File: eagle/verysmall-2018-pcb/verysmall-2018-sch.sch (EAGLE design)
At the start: 14 parts, among them IC1 7805, U1 ESP-WROOM-32, U2 AMS1117-3.3, U3 GY-521MPU6050

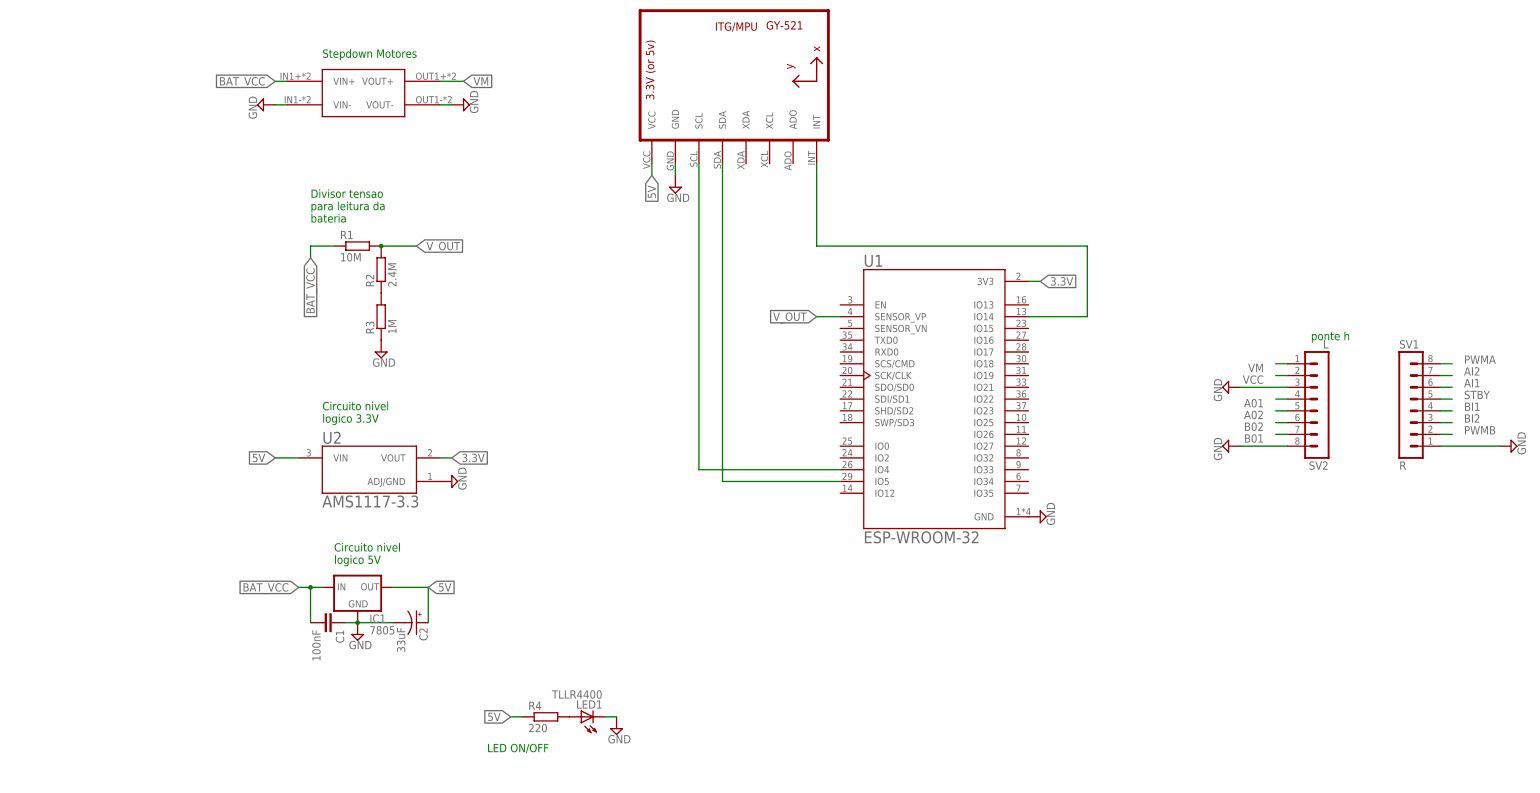
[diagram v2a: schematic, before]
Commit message: Adição dos pinos dos motores e do switch button
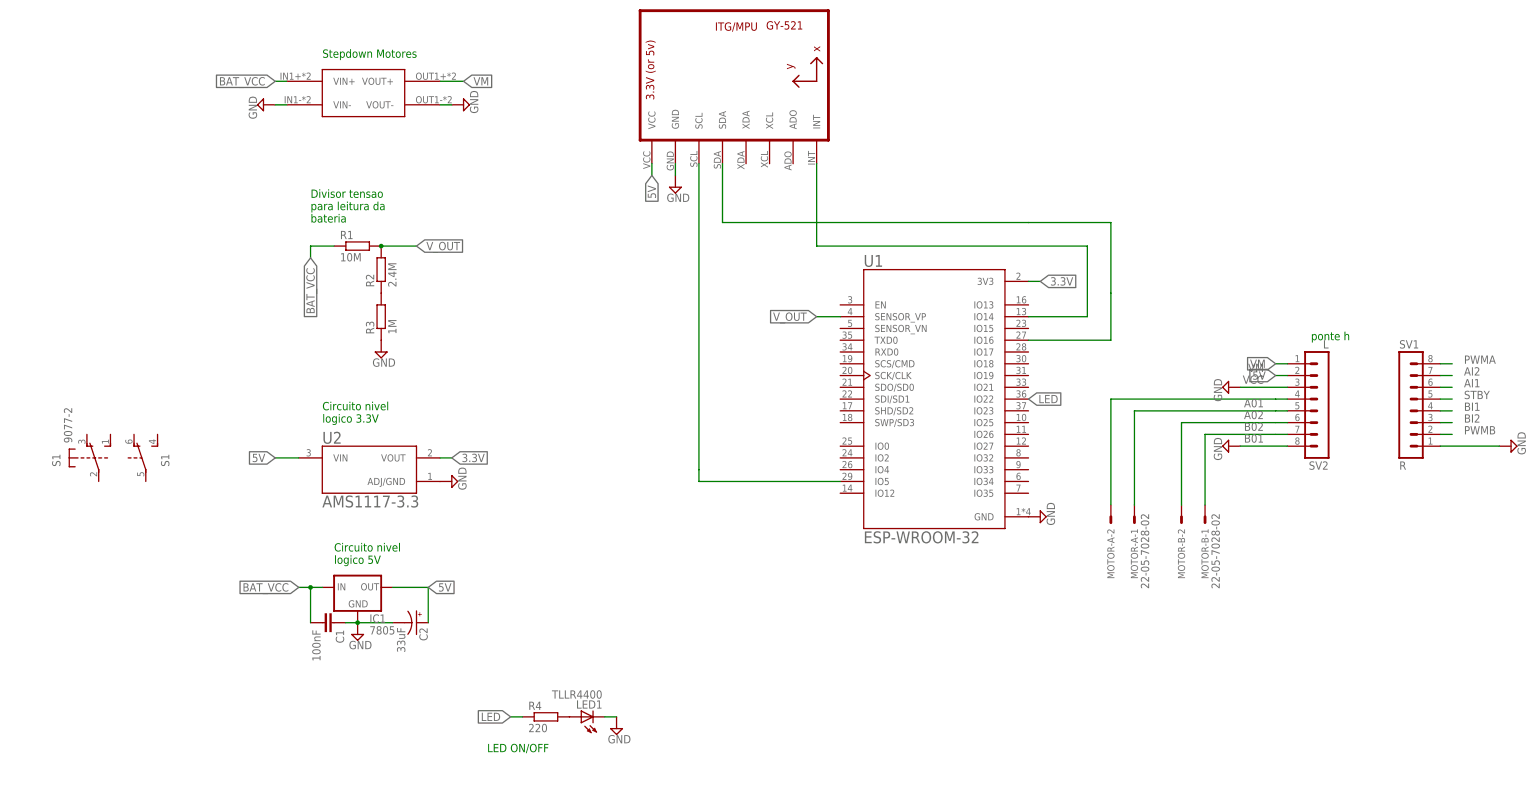
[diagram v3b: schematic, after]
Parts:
- added MOTOR-A, MOTOR-B: 22-05-7028-02, con-molex:22-05-7028-02
- added S1: 9077-2, switch-misc:9077-2
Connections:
- new net LED: R4.1
- net 5V: no longer R4.1
- net A01: now also MOTOR-A-2.S
- net A02: now also MOTOR-A-1.S
- net B01: now also MOTOR-B-1.S
- net B02: now also MOTOR-B-2.S
- net N$1: now also U1.IO5; no longer U1.IO4
- net N$3: now also U1.IO16; no longer U1.IO5
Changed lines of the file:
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@@
 <?xml version="1.0" encoding="utf-8"?>
 <!DOCTYPE eagle SYSTEM "eagle.dtd">
-<eagle version="9.1.2">
+<eagle version="9.1.0">
 <drawing>
 <settings>
@@
 <part name="R4" library="rcl" library_urn="urn:adsk.eagle:library:334" deviceset="R-EU_" device="0207/7" package3d_urn="urn:adsk.eagle:package:23493/1" value="220"/>
 <part name="SUPPLY11" library="supply2" library_urn="urn:adsk.eagle:library:372" deviceset="GND" device=""/>
+<part name="MOTOR-A" library="con-molex" library_urn="urn:adsk.eagle:library:165" deviceset="22-?-02" device="05-7028"/>
+<part name="MOTOR-B" library="con-molex" library_urn="urn:adsk.eagle:library:165" deviceset="22-?-02" device="05-7028"/>
+<part name="S1" library="switch-misc" library_urn="urn:adsk.eagle:library:376" deviceset="9077-2" device="" package3d_urn="urn:adsk.eagle:package:27425/1"/>
 </parts>
 <sheets>
@@
 <instance part="R4" gate="G$1" x="-63.5" y="2.54"/>
 <instance part="SUPPLY11" gate="GND" x="-48.26" y="0"/>
+<instance part="MOTOR-A" gate="-1" x="63.5" y="45.72" rot="R270"/>
+<instance part="MOTOR-A" gate="-2" x="58.42" y="45.72" rot="R270"/>
+<instance part="MOTOR-B" gate="-1" x="78.74" y="45.72" smashed="yes" rot="R270">
+<attribute name="NAME" x="77.978" y="43.18" size="1.524" layer="95" rot="R270"/>
+<attribute name="VALUE" x="80.137" y="46.482" size="1.778" layer="96" rot="R270"/>
+</instance>
+<instance part="MOTOR-B" gate="-2" x="73.66" y="45.72" rot="R270"/>
+<instance part="S1" gate="1" x="-160.02" y="58.42"/>
+<instance part="S1" gate="2" x="-149.86" y="58.42"/>
 </instances>
 <busses>
@@
 <pinref part="C2" gate="G$1" pin="+"/>
 <wire x1="-88.9" y1="22.86" x2="-88.9" y2="30.48" width="0.1524" layer="91"/>
+<label x="93.98" y="76.2" size="1.778" layer="95" rot="R180" xref="yes"/>
 </segment>
 <segment>
@@
 <label x="-40.64" y="119.38" size="1.778" layer="95" rot="R270" xref="yes"/>
 </segment>
-<segment>
-<pinref part="R4" gate="G$1" pin="1"/>
-<wire x1="-68.58" y1="2.54" x2="-71.12" y2="2.54" width="0.1524" layer="91"/>
-<label x="-71.12" y="2.54" size="1.778" layer="95" rot="R180" xref="yes"/>
-</segment>
 </net>
 <net name="N$1" class="0">
 <segment>
-<pinref part="U1" gate="G$1" pin="IO4"/>
-<wire x1="0" y1="55.88" x2="-30.48" y2="55.88" width="0.1524" layer="91"/>
 <pinref part="U3" gate="G$1" pin="SCL"/>
 <wire x1="-30.48" y1="55.88" x2="-30.48" y2="121.92" width="0.1524" layer="91"/>
-</segment>
-</net>
-<net name="N$3" class="0">
-<segment>
-<pinref part="U3" gate="G$1" pin="SDA"/>
 <pinref part="U1" gate="G$1" pin="IO5"/>
-<wire x1="-25.4" y1="121.92" x2="-25.4" y2="53.34" width="0.1524" layer="91"/>
-<wire x1="-25.4" y1="53.34" x2="0" y2="53.34" width="0.1524" layer="91"/>
+<wire x1="-30.48" y1="55.88" x2="-30.48" y2="53.34" width="0.1524" layer="91"/>
+<wire x1="-30.48" y1="53.34" x2="0" y2="53.34" width="0.1524" layer="91"/>
 </segment>
 </net>
@@
 <wire x1="-86.36" y1="139.7" x2="-81.28" y2="139.7" width="0.1524" layer="91"/>
 <label x="-81.28" y="139.7" size="1.778" layer="95" xref="yes"/>
+<label x="93.98" y="78.74" size="1.778" layer="95" rot="R180" xref="yes"/>
 </segment>
 <segment>
@@
 <wire x1="96.52" y1="71.12" x2="93.98" y2="71.12" width="0.1524" layer="91"/>
 <label x="91.44" y="71.12" size="1.778" layer="95" rot="R180"/>
+<pinref part="MOTOR-A" gate="-2" pin="S"/>
+<wire x1="58.42" y1="48.26" x2="58.42" y2="71.12" width="0.1524" layer="91"/>
+<wire x1="58.42" y1="71.12" x2="93.98" y2="71.12" width="0.1524" layer="91"/>
 </segment>
 </net>
@@
 <wire x1="96.52" y1="68.58" x2="93.98" y2="68.58" width="0.1524" layer="91"/>
 <label x="91.44" y="68.58" size="1.778" layer="95" rot="R180"/>
+<pinref part="MOTOR-A" gate="-1" pin="S"/>
+<wire x1="63.5" y1="48.26" x2="63.5" y2="68.58" width="0.1524" layer="91"/>
+<wire x1="63.5" y1="68.58" x2="93.98" y2="68.58" width="0.1524" layer="91"/>
 </segment>
 </net>
@@
 <wire x1="96.52" y1="66.04" x2="93.98" y2="66.04" width="0.1524" layer="91"/>
 <label x="91.44" y="66.04" size="1.778" layer="95" rot="R180"/>
+<pinref part="MOTOR-B" gate="-2" pin="S"/>
+<wire x1="73.66" y1="48.26" x2="73.66" y2="66.04" width="0.1524" layer="91"/>
+<wire x1="73.66" y1="66.04" x2="93.98" y2="66.04" width="0.1524" layer="91"/>
 </segment>
 </net>
@@
 <wire x1="96.52" y1="63.5" x2="93.98" y2="63.5" width="0.1524" layer="91"/>
 <label x="91.44" y="63.5" size="1.778" layer="95" rot="R180"/>
+<pinref part="MOTOR-B" gate="-1" pin="S"/>
+<wire x1="78.74" y1="48.26" x2="78.74" y2="63.5" width="0.1524" layer="91"/>
+<wire x1="78.74" y1="63.5" x2="93.98" y2="63.5" width="0.1524" layer="91"/>
 </segment>
 </net>
@@
 </segment>
 </net>
+<net name="LED" class="0">
+<segment>
+<pinref part="R4" gate="G$1" pin="1"/>
+<wire x1="-68.58" y1="2.54" x2="-71.12" y2="2.54" width="0.1524" layer="91"/>
+<label x="-71.12" y="2.54" size="1.778" layer="95" rot="R180" xref="yes"/>
+<label x="40.64" y="71.12" size="1.778" layer="95" xref="yes"/>
+</segment>
+</net>
+<net name="N$3" class="0">
+<segment>
+<pinref part="U3" gate="G$1" pin="SDA"/>
+<wire x1="-25.4" y1="121.92" x2="-25.4" y2="109.22" width="0.1524" layer="91"/>
+<wire x1="-25.4" y1="109.22" x2="40.64" y2="109.22" width="0.1524" layer="91"/>
+<wire x1="40.64" y1="109.22" x2="58.42" y2="109.22" width="0.1524" layer="91"/>
+<wire x1="58.42" y1="109.22" x2="58.42" y2="93.98" width="0.1524" layer="91"/>
+<pinref part="U1" gate="G$1" pin="IO16"/>
+<wire x1="58.42" y1="93.98" x2="58.42" y2="83.82" width="0.1524" layer="91"/>
+<wire x1="58.42" y1="83.82" x2="40.64" y2="83.82" width="0.1524" layer="91"/>
+</segment>
+</net>

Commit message: Esquematico pronto
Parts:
- added BAT, CHG, RX-TX: 22-05-7028-02, con-molex:22-05-7028-02
- added C3, C5: 100nF, rcl:C-EU075-032X103
- added C4, C6: 10uF, rcl:CPOL-USE2-5
- added Q1: BC548, transistor-npn:BC548
- added R5: 2K2, eagle-ltspice:R0207/10
- added SG1: F/HMB, buzzer:F/HMB
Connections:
- new net BUZZER: R5.1
- new net N$10: U1.IO27
- new net N$11: U1.IO25
- new net N$12: U1.IO32
- new net N$13: U1.IO34
- new net N$14: U1.IO35
- new net N$15: RX-TX-2.S, U1.TXD0
- new net N$16: RX-TX-1.S, U1.RXD0
- new net N$17: Q1.C, SG1.-
- new net N$18: Q1.B, R5.2
- new net N$6: CHG-2.S, S11.S, S12.S
- new net N$7: S11.O, S12.O
- new net N$8: BAT-2.S, S11.P, S12.P
- new net N$9: U1.IO12
- net 3.3V: now also C4.+
- net 5V: now also C5.2
- net BAT_VCC: now also C3.2
- net GND: now also BAT-1.S, C3.1, C4.-, C5.1, C6.-, CHG-1.S, Q1.E
- net VM: now also C6.+

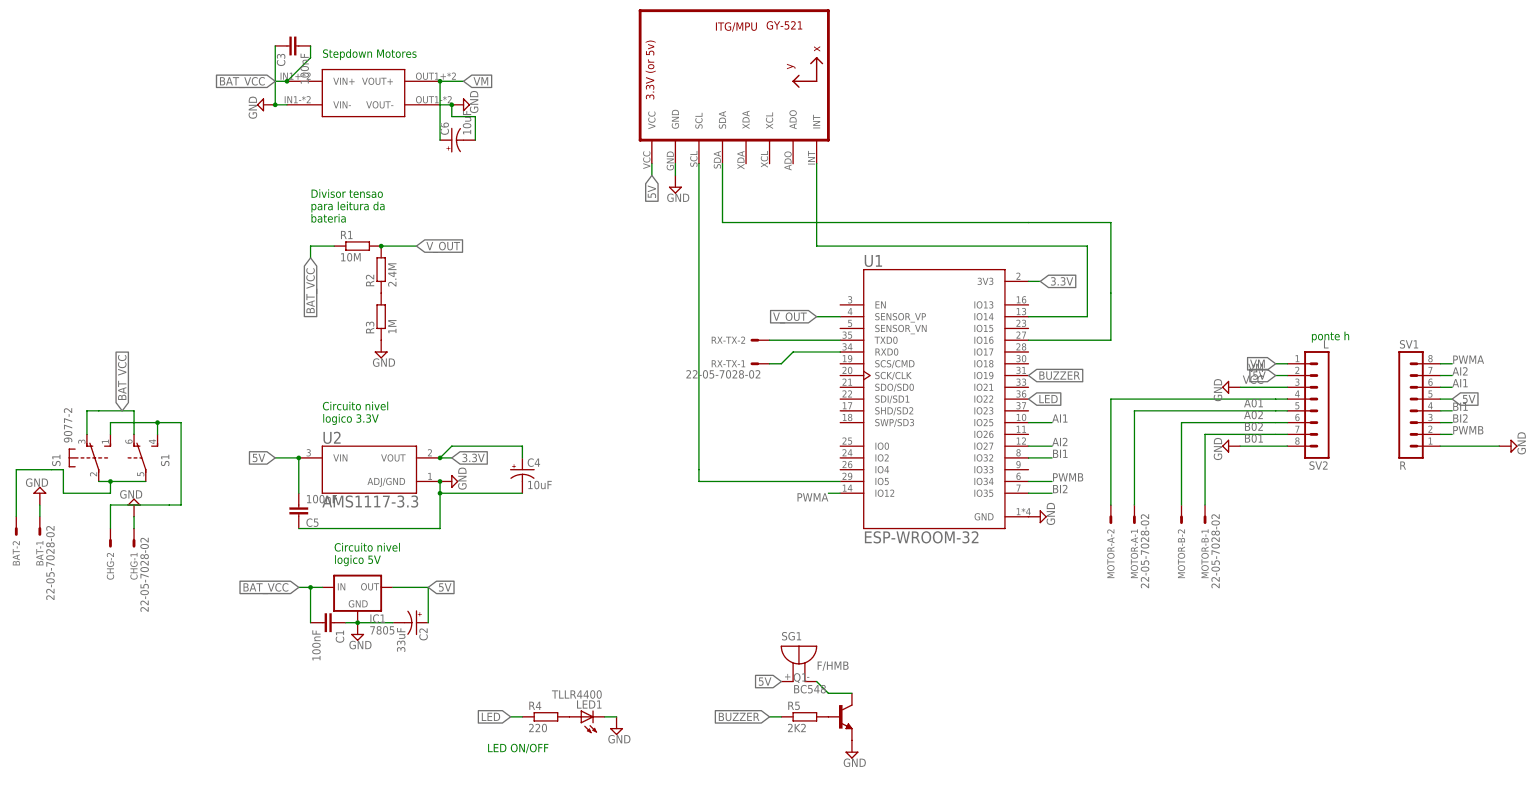
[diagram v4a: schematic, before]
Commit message: ajuste de lable
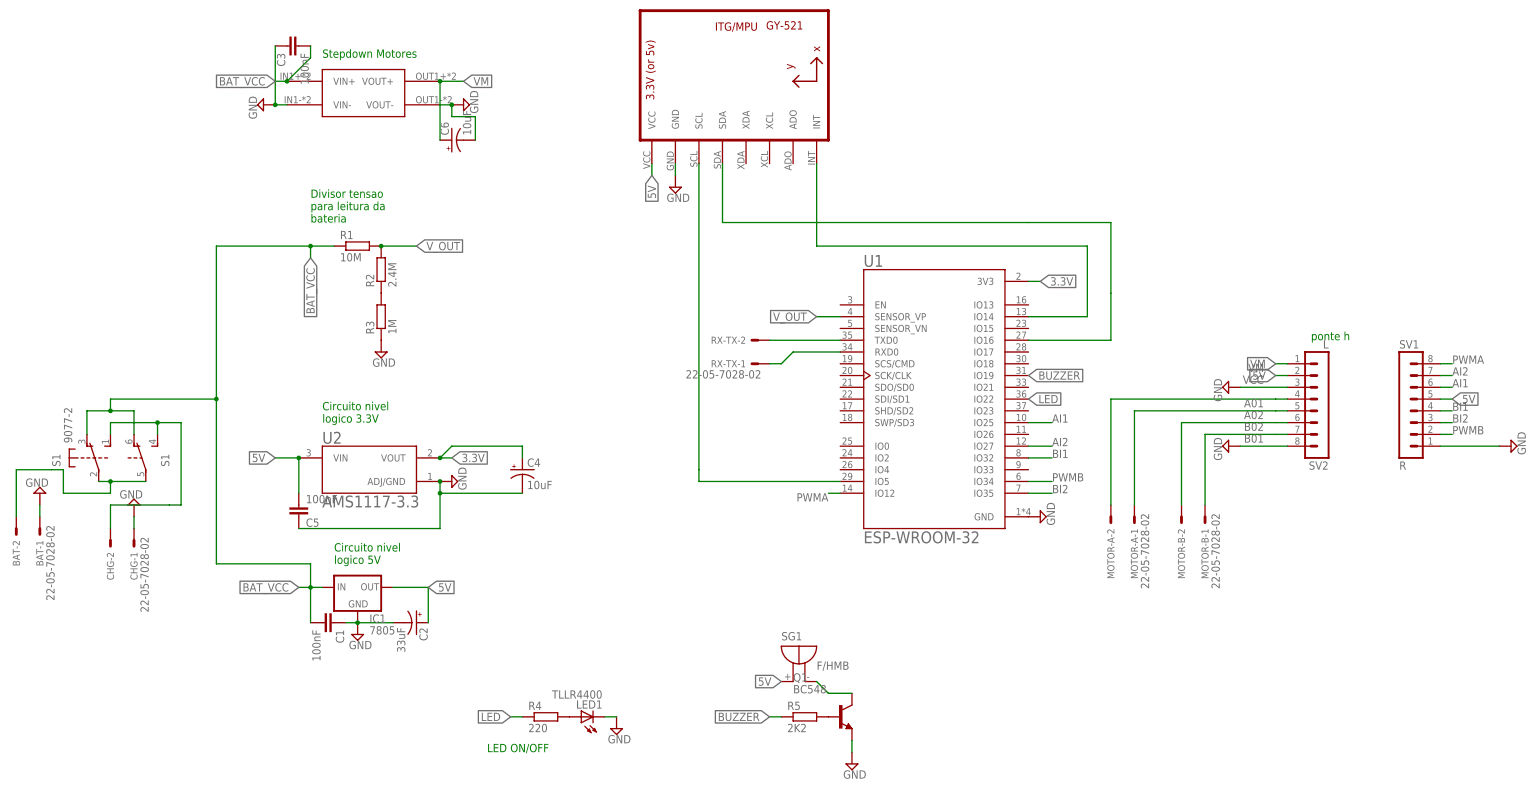
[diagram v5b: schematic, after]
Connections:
- removed net N$7: S11.O, S12.O
- net BAT_VCC: now also S11.O, S12.O
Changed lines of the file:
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@@
 <instance part="SG1" gate="G$1" x="-10.16" y="12.7"/>
 <instance part="Q1" gate="G$1" x="0" y="2.54"/>
-<instance part="SUPPLY14" gate="GND" x="2.54" y="-5.08"/>
+<instance part="SUPPLY14" gate="GND" x="2.54" y="-7.62"/>
 <instance part="R5" gate="G$1" x="-7.62" y="2.54"/>
 </instances>
@@
 <pinref part="Q1" gate="G$1" pin="E"/>
 <pinref part="SUPPLY14" gate="GND" pin="GND"/>
+<wire x1="2.54" y1="-5.08" x2="2.54" y2="-2.54" width="0.1524" layer="91"/>
 </segment>
 </net>
@@
 </net>
 <net name="BAT_VCC" class="0">
-<segment>
-<pinref part="R1" gate="G$1" pin="1"/>
-<wire x1="-109.22" y1="104.14" x2="-114.3" y2="104.14" width="0.1524" layer="91"/>
-<label x="-114.3" y="101.6" size="1.778" layer="95" rot="R270" xref="yes"/>
-<wire x1="-114.3" y1="101.6" x2="-114.3" y2="104.14" width="0.1524" layer="91"/>
-</segment>
 <segment>
 <pinref part="IC1" gate="A" pin="IN"/>
@@
 <wire x1="-114.3" y1="22.86" x2="-114.3" y2="30.48" width="0.1524" layer="91"/>
 <junction x="-114.3" y="30.48"/>
-<label x="-154.94" y="68.58" size="1.778" layer="95" rot="R90" xref="yes"/>
+<wire x1="-134.62" y1="104.14" x2="-134.62" y2="71.12" width="0.1524" layer="91"/>
+<wire x1="-134.62" y1="71.12" x2="-134.62" y2="35.56" width="0.1524" layer="91"/>
+<wire x1="-134.62" y1="35.56" x2="-114.3" y2="35.56" width="0.1524" layer="91"/>
+<wire x1="-114.3" y1="35.56" x2="-114.3" y2="30.48" width="0.1524" layer="91"/>
+<pinref part="R1" gate="G$1" pin="1"/>
+<wire x1="-109.22" y1="104.14" x2="-114.3" y2="104.14" width="0.1524" layer="91"/>
+<label x="-114.3" y="101.6" size="1.778" layer="95" rot="R270" xref="yes"/>
+<wire x1="-114.3" y1="101.6" x2="-114.3" y2="104.14" width="0.1524" layer="91"/>
+<wire x1="-134.62" y1="104.14" x2="-114.3" y2="104.14" width="0.1524" layer="91"/>
+<junction x="-114.3" y="104.14"/>
+<pinref part="S1" gate="1" pin="O"/>
+<wire x1="-162.56" y1="68.58" x2="-162.56" y2="63.5" width="0.1524" layer="91"/>
+<wire x1="-157.48" y1="68.58" x2="-162.56" y2="68.58" width="0.1524" layer="91"/>
+<wire x1="-157.48" y1="68.58" x2="-157.48" y2="71.12" width="0.1524" layer="91"/>
+<junction x="-157.48" y="68.58"/>
+<pinref part="S1" gate="2" pin="O"/>
+<wire x1="-152.4" y1="63.5" x2="-152.4" y2="68.58" width="0.1524" layer="91"/>
+<wire x1="-152.4" y1="68.58" x2="-157.48" y2="68.58" width="0.1524" layer="91"/>
+<wire x1="-157.48" y1="71.12" x2="-134.62" y2="71.12" width="0.1524" layer="91"/>
+<junction x="-134.62" y="71.12"/>
 </segment>
 <segment>
@@
 </segment>
 </net>
-<net name="N$7" class="0">
-<segment>
-<pinref part="S1" gate="2" pin="O"/>
-<wire x1="-152.4" y1="63.5" x2="-152.4" y2="68.58" width="0.1524" layer="91"/>
-<wire x1="-152.4" y1="68.58" x2="-160.02" y2="68.58" width="0.1524" layer="91"/>
-<pinref part="S1" gate="1" pin="O"/>
-<wire x1="-160.02" y1="68.58" x2="-162.56" y2="68.58" width="0.1524" layer="91"/>
-<wire x1="-162.56" y1="68.58" x2="-162.56" y2="63.5" width="0.1524" layer="91"/>
-</segment>
-</net>
 <net name="N$8" class="0">
 <segment>
@@
 </sheet>
 </sheets>
+<errors>
+</errors>
 </schematic>
 </drawing>
